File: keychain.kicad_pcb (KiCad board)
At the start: 2 copper layers, 41 x 39 mm, 49 parts, among them P1 CAP_SLIDER, P2 VBAT, P3 CONN_01X04, P4 CONN_01X05, SW1 ~RESET~, SW2 BOOT, SW3 USR1, SW4 USR2, U1 EFM32TG110

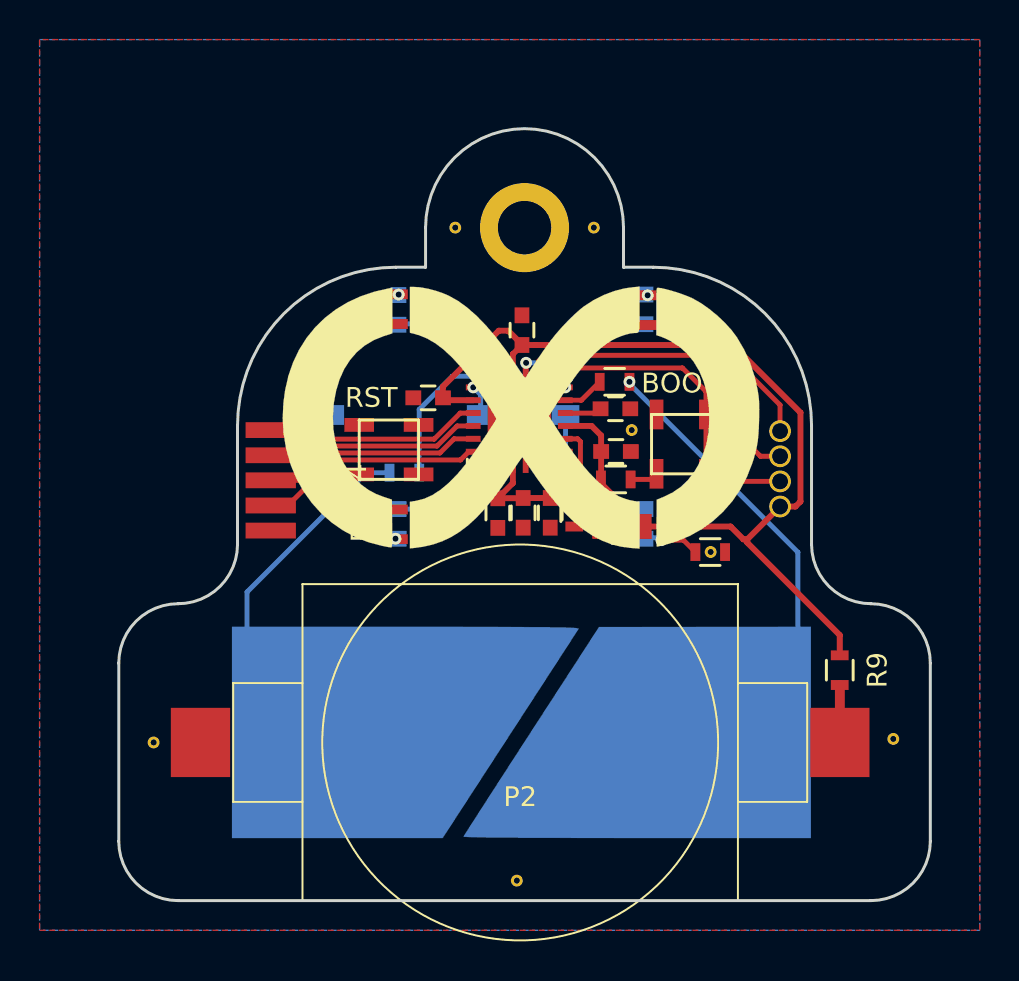
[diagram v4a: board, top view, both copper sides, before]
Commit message: move capsense resistor to front side and reroute
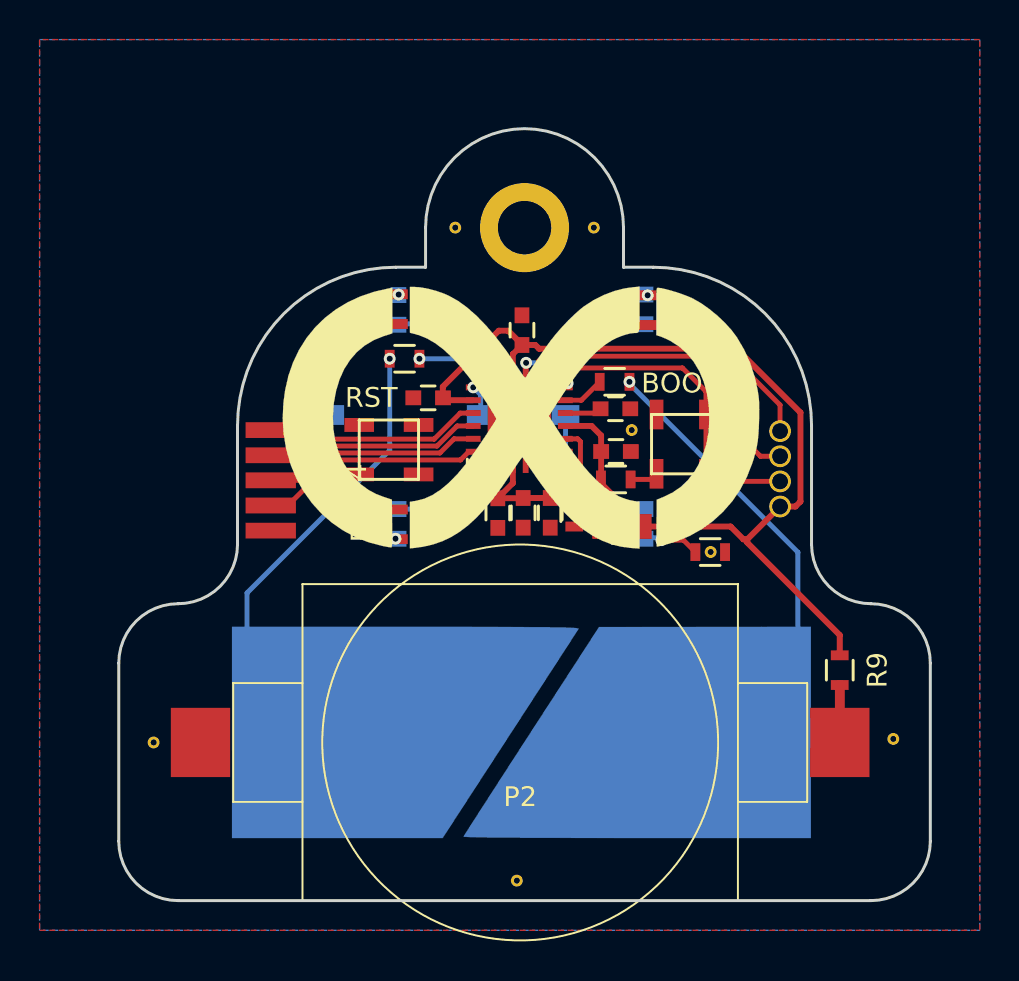
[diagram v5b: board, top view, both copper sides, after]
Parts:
- R8: moved to F.Cu
- moved R8 5.76 mm to (143.4, 88.6)
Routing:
- net Net-(P1-Pad1): track 16.9 -> 22.0 mm, vias 0 -> 1
- net CAP_S_1: track 11.5 -> 8.26 mm, vias 1 -> 2
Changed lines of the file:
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@@
   (general
     (links 80)
-    (no_connects 4)
+    (no_connects 3)
     (area 128.924999 76.924999 170.075001 116.075001)
     (thickness 1.6)
     (drawings 20)
-    (tracks 154)
+    (tracks 159)
     (zones 0)
     (modules 49)
@@
     (47 F.CrtYd user hide)
     (48 B.Fab user hide)
-    (49 F.Fab user hide)
+    (49 F.Fab user)
   )
   (setup
@@
     )
   )
-  (module Resistors_SMD:R_0603 (layer B.Cu)
-    (at 143.42872 94.38132 180)
+  (module Resistors_SMD:R_0603 (layer F.Cu)
+    (at 143.43888 88.62314 180)
     (descr "Resistor SMD 0603, reflow soldering, Vishay (see dcrcw.pdf)")
     (tags "resistor 0603")
     (attr smd)
-    (fp_text reference R8 (at -0.5156 -1.3377 180) (layer Cmts.User)
-      (effects (font (size 1 1) (thickness 0.15)))
-    )
-    (fp_text value 100R (at 0 -1.9 180) (layer B.Fab)
-      (effects (font (size 1 1) (thickness 0.15)) (justify mirror))
-    )
-    (fp_line (start -0.5 0.675) (end 0.5 0.675) (layer B.SilkS) (width 0.15))
-    (fp_line (start 0.5 -0.675) (end -0.5 -0.675) (layer B.SilkS) (width 0.15))
-    (fp_line (start 1.3 0.8) (end 1.3 -0.8) (layer B.CrtYd) (width 0.05))
-    (fp_line (start -1.3 0.8) (end -1.3 -0.8) (layer B.CrtYd) (width 0.05))
-    (fp_line (start -1.3 -0.8) (end 1.3 -0.8) (layer B.CrtYd) (width 0.05))
-    (fp_line (start -1.3 0.8) (end 1.3 0.8) (layer B.CrtYd) (width 0.05))
-    (pad 2 smd rect (at 0.75 0 180) (size 0.5 0.9) (layers B.Cu B.Paste B.Mask)
+    (fp_text reference R8 (at -0.5156 1.3377 180) (layer Cmts.User)
+      (effects (font (size 1 1) (thickness 0.15)))
+    )
+    (fp_text value 100R (at 0 1.9 180) (layer F.Fab)
+      (effects (font (size 1 1) (thickness 0.15)))
+    )
+    (fp_line (start -0.5 -0.675) (end 0.5 -0.675) (layer F.SilkS) (width 0.15))
+    (fp_line (start 0.5 0.675) (end -0.5 0.675) (layer F.SilkS) (width 0.15))
+    (fp_line (start 1.3 -0.8) (end 1.3 0.8) (layer F.CrtYd) (width 0.05))
+    (fp_line (start -1.3 -0.8) (end -1.3 0.8) (layer F.CrtYd) (width 0.05))
+    (fp_line (start -1.3 0.8) (end 1.3 0.8) (layer F.CrtYd) (width 0.05))
+    (fp_line (start -1.3 -0.8) (end 1.3 -0.8) (layer F.CrtYd) (width 0.05))
+    (pad 2 smd rect (at 0.75 0 180) (size 0.5 0.9) (layers F.Cu F.Paste F.Mask)
       (net 15 "Net-(P1-Pad1)"))
-    (pad 1 smd rect (at -0.75 0 180) (size 0.5 0.9) (layers B.Cu B.Paste B.Mask)
+    (pad 1 smd rect (at -0.75 0 180) (size 0.5 0.9) (layers F.Cu F.Paste F.Mask)
       (net 20 CAP_S_1))
     (model Resistors_SMD.3dshapes/R_0603.wrl
@@
   (module smallbutton:Tactile_Push_Button_SMD_3x3x1.5mm.kicad_mod (layer F.Cu)
     (at 157.4165 92.9386 90)
-    (fp_text reference SW2 (at 0 -2.54 90) (layer Cmts.User)
+    (fp_text reference SW2 (at 0 -0.01778 90) (layer Cmts.User)
       (effects (font (size 1 1) (thickness 0.15)))
     )
@@
   (gr_arc (start 143 92) (end 135 92) (angle 90) (layer Edge.Cuts) (width 0.15))
   (gr_arc (start 156 92) (end 156 84) (angle 90) (layer Edge.Cuts) (width 0.15))
+  (segment (start 162.41 96.089999) (end 163.187817 96.089999) (width 0.3) (layer F.Cu) (net 1))
+  (segment (start 163.187817 96.089999) (end 163.44 95.837816) (width 0.3) (layer F.Cu) (net 1))
+  (segment (start 163.44 95.837816) (end 163.44 91.343231) (width 0.3) (layer F.Cu) (net 1))
+  (segment (start 163.44 91.343231) (end 160.214449 88.11768) (width 0.3) (layer F.Cu) (net 1))
+  (segment (start 160.214449 88.11768) (end 150.23268 88.11768) (width 0.3) (layer F.Cu) (net 1))
+  (segment (start 150.23268 88.11768) (end 150.045 87.93) (width 0.3) (layer F.Cu) (net 1))
+  (segment (start 150.045 87.93) (end 149.37 87.93) (width 0.3) (layer F.Cu) (net 1))
+  (segment (start 145.37 90.035996) (end 145.37 90.75) (width 0.3) (layer F.Cu) (net 1))
+  (segment (start 148.197636 87.20836) (end 145.37 90.035996) (width 0.3) (layer F.Cu) (net 1))
+  (segment (start 148.67336 87.20836) (end 148.197636 87.20836) (width 0.3) (layer F.Cu) (net 1))
+  (segment (start 149.37 87.905) (end 148.67336 87.20836) (width 0.3) (layer F.Cu) (net 1))
   (segment (start 149.37 87.93) (end 149.37 87.905) (width 0.3) (layer F.Cu) (net 1))
-  (segment (start 149.37 87.905) (end 148.67336 87.20836) (width 0.3) (layer F.Cu) (net 1))
-  (segment (start 148.67336 87.20836) (end 148.197636 87.20836) (width 0.3) (layer F.Cu) (net 1))
-  (segment (start 148.197636 87.20836) (end 145.37 90.035996) (width 0.3) (layer F.Cu) (net 1))
-  (segment (start 145.37 90.035996) (end 145.37 90.75) (width 0.3) (layer F.Cu) (net 1))
   (segment (start 160.749999 97.75) (end 160.749999 97.910399) (width 0.3) (layer F.Cu) (net 1))
   (segment (start 160.749999 97.910399) (end 165.42512 102.58552) (width 0.3) (layer F.Cu) (net 1))
@@
   (segment (start 162.41 96.089999) (end 160.749999 97.75) (width 0.3) (layer F.Cu) (net 1))
   (segment (start 159.91 97.1) (end 155.42 97.1) (width 0.3) (layer F.Cu) (net 1))
-  (segment (start 162.41 96.089999) (end 163.187817 96.089999) (width 0.3) (layer F.Cu) (net 1))
-  (segment (start 163.187817 96.089999) (end 163.44 95.837816) (width 0.3) (layer F.Cu) (net 1))
-  (segment (start 163.44 91.343231) (end 160.026769 87.93) (width 0.3) (layer F.Cu) (net 1))
-  (segment (start 163.44 95.837816) (end 163.44 91.343231) (width 0.3) (layer F.Cu) (net 1))
   (segment (start 155.42 97.1) (end 155.42 96.975) (width 0.3) (layer F.Cu) (net 1))
   (segment (start 155.42 96.975) (end 153.36 94.915) (width 0.3) (layer F.Cu) (net 1))
@@
   (segment (start 153.37 93.31) (end 153.37 94.71) (width 0.3) (layer F.Cu) (net 1))
   (segment (start 153.37 94.71) (end 153.36 94.72) (width 0.3) (layer F.Cu) (net 1))
-  (segment (start 150.045 87.93) (end 149.37 87.93) (width 0.3) (layer F.Cu) (net 1))
-  (segment (start 160.026769 87.93) (end 150.045 87.93) (width 0.3) (layer F.Cu) (net 1))
   (segment (start 148.91 88.39) (end 149.37 87.93) (width 0.3) (layer F.Cu) (net 1))
   (segment (start 153.37 92.5) (end 152.89 92.02) (width 0.3) (layer F.Cu) (net 1))
@@
   (segment (start 153.12 91.37) (end 153.34 91.15) (width 0.25) (layer F.Cu) (net 3))
   (segment (start 150.21 89.37) (end 150.21 88.745) (width 0.25) (layer F.Cu) (net 5))
-  (segment (start 150.21 88.745) (end 150.505011 88.449989) (width 0.25) (layer F.Cu) (net 5))
-  (segment (start 150.505011 88.449989) (end 159.900189 88.449989) (width 0.25) (layer F.Cu) (net 5))
-  (segment (start 159.900189 88.449989) (end 162.4076 90.9574) (width 0.25) (layer F.Cu) (net 5))
+  (segment (start 150.21 88.745) (end 150.45886 88.49614) (width 0.25) (layer F.Cu) (net 5))
   (segment (start 162.4076 90.9574) (end 162.4076 92.277598) (width 0.25) (layer F.Cu) (net 5))
+  (segment (start 150.45886 88.49614) (end 159.94634 88.49614) (width 0.25) (layer F.Cu) (net 5))
+  (segment (start 159.94634 88.49614) (end 162.4076 90.9574) (width 0.25) (layer F.Cu) (net 5))
   (segment (start 162.4076 92.277598) (end 162.41 92.279998) (width 0.25) (layer F.Cu) (net 5))
   (segment (start 158.6665 91.4386) (end 158.6665 90.27954) (width 0.25) (layer F.Cu) (net 6))
@@
   (via (at 149.58 88.830002) (size 0.6) (drill 0.3) (layers F.Cu B.Cu) (net 13))
   (segment (start 153.42 97.1) (end 152.01 97.1) (width 0.25) (layer F.Cu) (net 14))
-  (segment (start 135.48 100.41) (end 141.50868 94.38132) (width 0.25) (layer B.Cu) (net 15))
-  (segment (start 141.50868 94.38132) (end 142.67872 94.38132) (width 0.25) (layer B.Cu) (net 15))
-  (segment (start 135.48 107.64) (end 135.48 100.41) (width 0.25) (layer B.Cu) (net 15))
+  (segment (start 135.48 107.64) (end 135.48 100.45552) (width 0.25) (layer B.Cu) (net 15))
+  (segment (start 135.48 100.45552) (end 142.68888 93.24664) (width 0.25) (layer B.Cu) (net 15))
+  (segment (start 142.68888 93.24664) (end 142.68888 88.62314) (width 0.25) (layer B.Cu) (net 15))
+  (via (at 142.68888 88.62314) (size 0.6) (drill 0.3) (layers F.Cu B.Cu) (net 15))
   (segment (start 154.8 89.79) (end 154.8 89.89) (width 0.25) (layer B.Cu) (net 16))
   (segment (start 154.8 89.89) (end 163.31 98.4) (width 0.25) (layer B.Cu) (net 16))
@@
   (segment (start 152.37 90.72) (end 153.3 89.79) (width 0.25) (layer F.Cu) (net 19))
   (segment (start 151.562312 90.717688) (end 151.56 90.72) (width 0.25) (layer F.Cu) (net 19))
-  (segment (start 145.85188 89.5096) (end 150.9996 89.5096) (width 0.25) (layer B.Cu) (net 20))
-  (segment (start 150.9996 89.5096) (end 151.56 90.07) (width 0.25) (layer B.Cu) (net 20))
-  (via (at 151.56 90.07) (size 0.6) (drill 0.3) (layers F.Cu B.Cu) (net 20))
-  (segment (start 144.17872 91.18276) (end 145.85188 89.5096) (width 0.25) (layer B.Cu) (net 20))
-  (segment (start 144.17872 94.38132) (end 144.17872 91.18276) (width 0.25) (layer B.Cu) (net 20))
+  (segment (start 147.944561 89.560121) (end 147.00758 88.62314) (width 0.25) (layer B.Cu) (net 20))
+  (segment (start 147.00758 88.62314) (end 144.18888 88.62314) (width 0.25) (layer B.Cu) (net 20))
+  (via (at 144.18888 88.62314) (size 0.6) (drill 0.3) (layers F.Cu B.Cu) (net 20))
+  (segment (start 151.6761 89.86012) (end 151.376101 89.560121) (width 0.25) (layer B.Cu) (net 20))
+  (segment (start 151.376101 89.560121) (end 147.944561 89.560121) (width 0.25) (layer B.Cu) (net 20))
+  (segment (start 151.56 90.07) (end 151.56 89.97622) (width 0.25) (layer F.Cu) (net 20))
+  (segment (start 151.56 89.97622) (end 151.6761 89.86012) (width 0.25) (layer F.Cu) (net 20))
+  (via (at 151.6761 89.86012) (size 0.6) (drill 0.3) (layers F.Cu B.Cu) (net 20))
   (segment (start 148.91 94.02) (end 148.91 94.91) (width 0.3) (layer F.Cu) (net 21))
   (segment (start 148.15 95.67) (end 149.42 95.67) (width 0.3) (layer F.Cu) (net 21))

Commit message: Rotate buttons to look nicer, fix missing reset connection
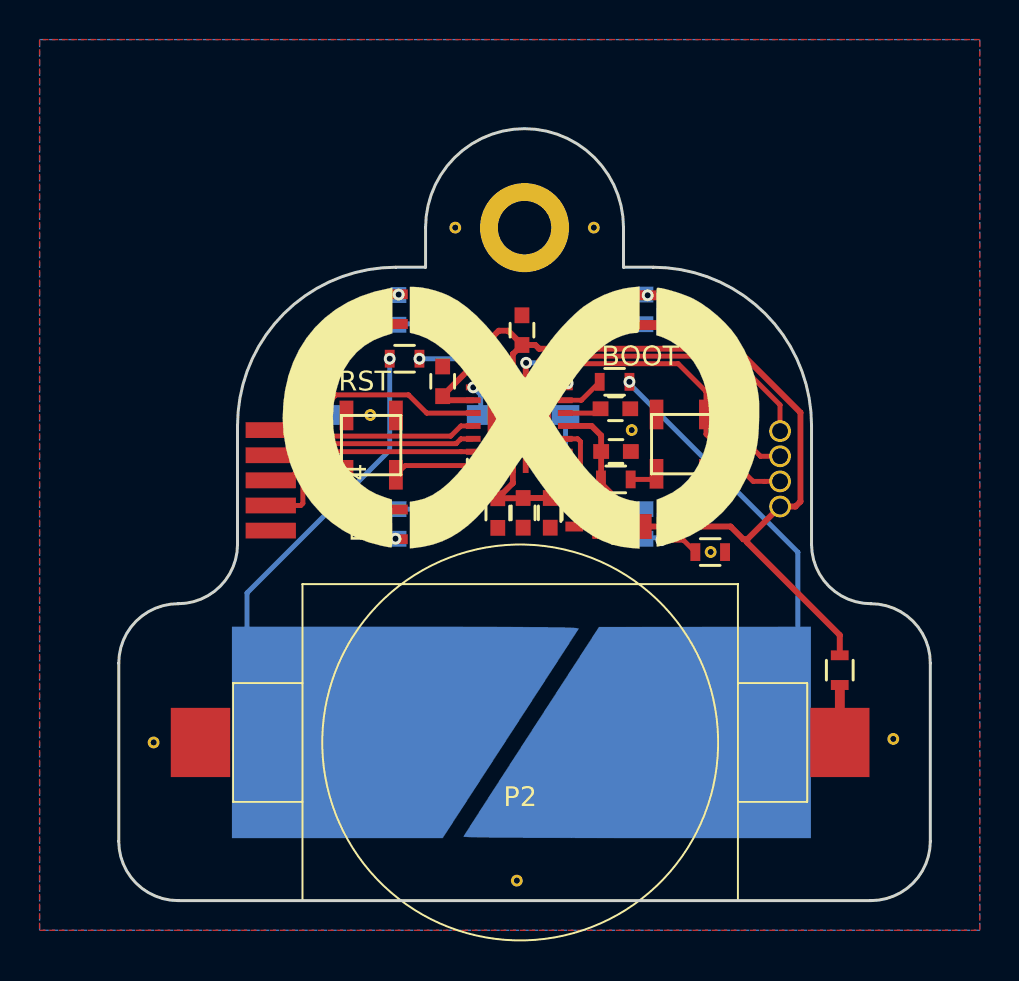
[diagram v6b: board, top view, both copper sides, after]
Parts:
- added REF**: VIA_0.6mm, GNDVIA:GND_VIA_0.6mm, F.Cu at (142.6, 91.4)
- moved C2 1.11 mm to (145.4, 89.8), turned to 90 degrees
- moved SW1 0.92 mm to (141.8, 93.0), turned to 90 degrees
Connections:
- net Net-(P4-Pad2) renamed /US1_CS
- net Net-(P4-Pad3) renamed /US1_CLK
- net Net-(P4-Pad4) renamed /US1_RX
- net Net-(P4-Pad5) renamed /US1_TX
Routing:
- net /~RST~: track 0.00 -> 4.80 mm
- net SWCLK: track 16.5 -> 15.5 mm
- net /US1_CS: track 11.4 -> 12.1 mm
